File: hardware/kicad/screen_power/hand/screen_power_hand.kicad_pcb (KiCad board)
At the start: 2 copper layers, 68 x 76 mm, 48 parts, among them J1 AUX 5V INPUT, J101 PI USB / XH4, J102 TOUCH / XH4, J103 SCREEN 1 POWER, J2 GPIO17 / GND, J201 PI USB / XH4, J202 TOUCH / XH4, J203 SCREEN 2 POWER, K101 IM02TS, K201 IM02TS, Q1 2N3904, Q101 TN0702, Q2 2N3906, Q201 TN0702, Q3 SUP70101EL, Q4 SUP70101EL, U1 LMC7660IN, U2 TLP627M

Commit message: fix(hardware): finish revision M USB routing and manufacturing package
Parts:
- added Q102: TN0702, TO-92_Inline_Wide, F.Cu at (31.7, 45.7)
- added Q202: TN0702, TO-92_Inline_Wide, F.Cu at (31.7, 70.7)
- added R101: 10k 1%, R_Axial_DIN0207_L6.3mm_D2.5mm_P10.16mm_Horizontal, F.Cu at (22.1, 49.0)
- added R102: 100k 1%, R_Axial_DIN0207_L6.3mm_D2.5mm_P10.16mm_Horizontal, F.Cu at (32.8, 55.6)
- added R201: 10k 1%, R_Axial_DIN0207_L6.3mm_D2.5mm_P10.16mm_Horizontal, F.Cu at (9.42, 73.3)
- added R202: 100k 1%, R_Axial_DIN0207_L6.3mm_D2.5mm_P10.16mm_Horizontal, F.Cu at (22.1, 73.5)
- added TP101: SHIELD, TestPoint_THTPad_D2.0mm_Drill1.0mm, F.Cu at (13.5, 31.5)
- added TP102: SHIELD, TestPoint_THTPad_D2.0mm_Drill1.0mm, F.Cu at (51.5, 32.0)
- added TP201: SHIELD, TestPoint_THTPad_D2.0mm_Drill1.0mm, F.Cu at (13.5, 56.5)
- added TP202: SHIELD, TestPoint_THTPad_D2.0mm_Drill1.0mm, F.Cu at (51.5, 57.0)
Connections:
- C101 pad 1: HOST1_5V -> AUX_5V
- C201 pad 1: HOST2_5V -> AUX_5V
- D101 pad 1: HOST1_5V -> AUX_5V
- D201 pad 1: HOST2_5V -> AUX_5V
- K101 pad 1: HOST1_5V -> AUX_5V
- K201 pad 1: HOST2_5V -> AUX_5V
- Q101 pad 3: S1_DATA_COIL_LOW -> S1_RELAY_STACK
- Q201 pad 3: S2_DATA_COIL_LOW -> S2_RELAY_STACK
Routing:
- net AUX_5V: track 138.6 -> 200.5 mm, vias 0 -> 4
- net S2_HOST_PRESENT: track 0.00 -> 14.4 mm
- net S1_HOST_PRESENT: track 0.00 -> 13.7 mm
- net HOST2_5V: track 21.0 -> 9.45 mm
- net DATA_ENABLE: track 66.6 -> 76.8 mm
- net POWER_GATE: track 22.4 -> 28.1 mm
- net S2_RELAY_STACK: track 0.00 -> 4.69 mm
- net S1_RELAY_STACK: track 0.00 -> 4.69 mm
- net S1_DATA_COIL_LOW: track 29.4 -> 26.4 mm
- net S2_DATA_COIL_LOW: track 29.4 -> 26.4 mm
- net BUFFER_BASE: track 9.53 -> 11.4 mm
- net HOST1_5V: track 21.0 -> 19.2 mm
- net CONTROL_SINK: track 72.1 -> 71.3 mm
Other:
- board text added: "REV M"
- board text added: "SEGNO SCREEN POWER / REV M"
- board text removed: "REV L"
- board text removed: "SEGNO SCREEN POWER"
- board text removed: "SEGNO SCREEN POWER / REV L"

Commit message: fix(hardware): close Claude PCB review findings
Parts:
- R2: value 100k 1% -> 4.7k 1%
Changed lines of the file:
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@@
 			)
 		)
-		(property "Value" "100k 1%"
+		(property "Value" "4.7k 1%"
 			(at 5.08 2.37 0)
 			(layer "F.Fab")

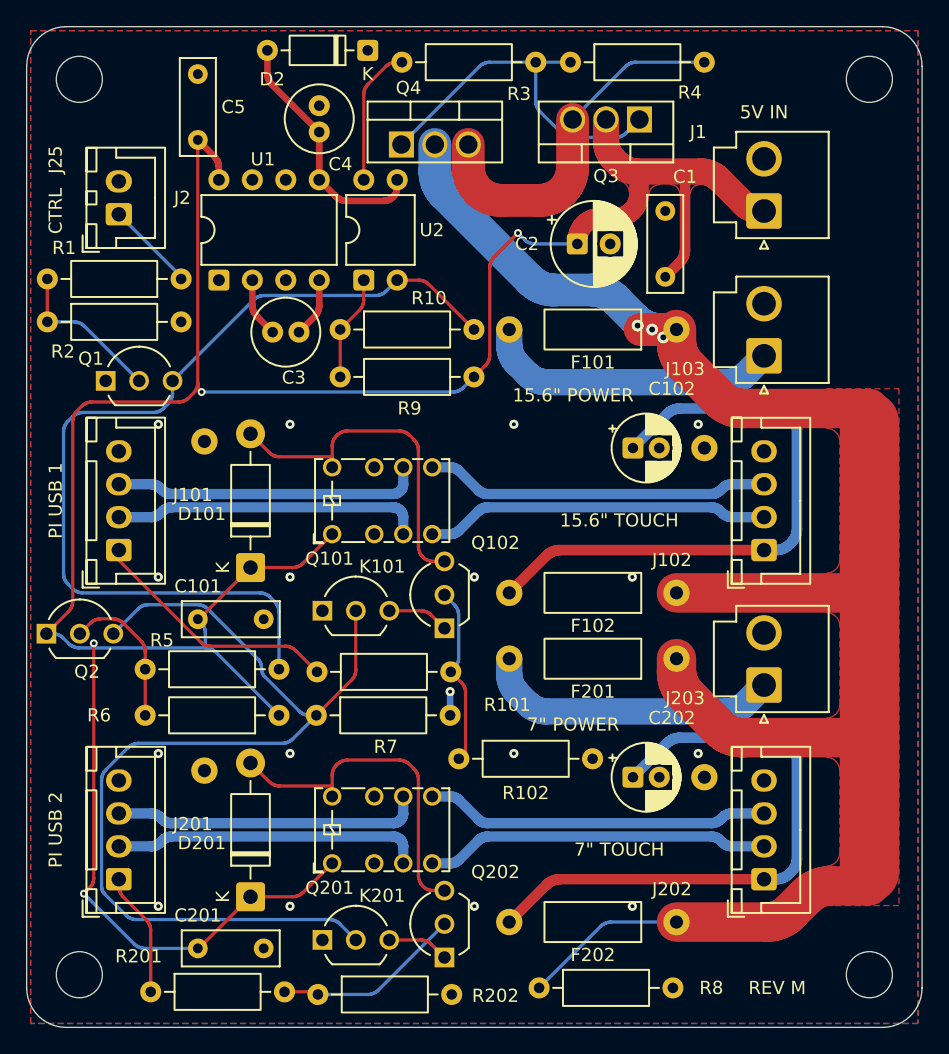
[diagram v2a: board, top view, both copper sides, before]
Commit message: feat(hardware): lower screen power cost and finish copper contours
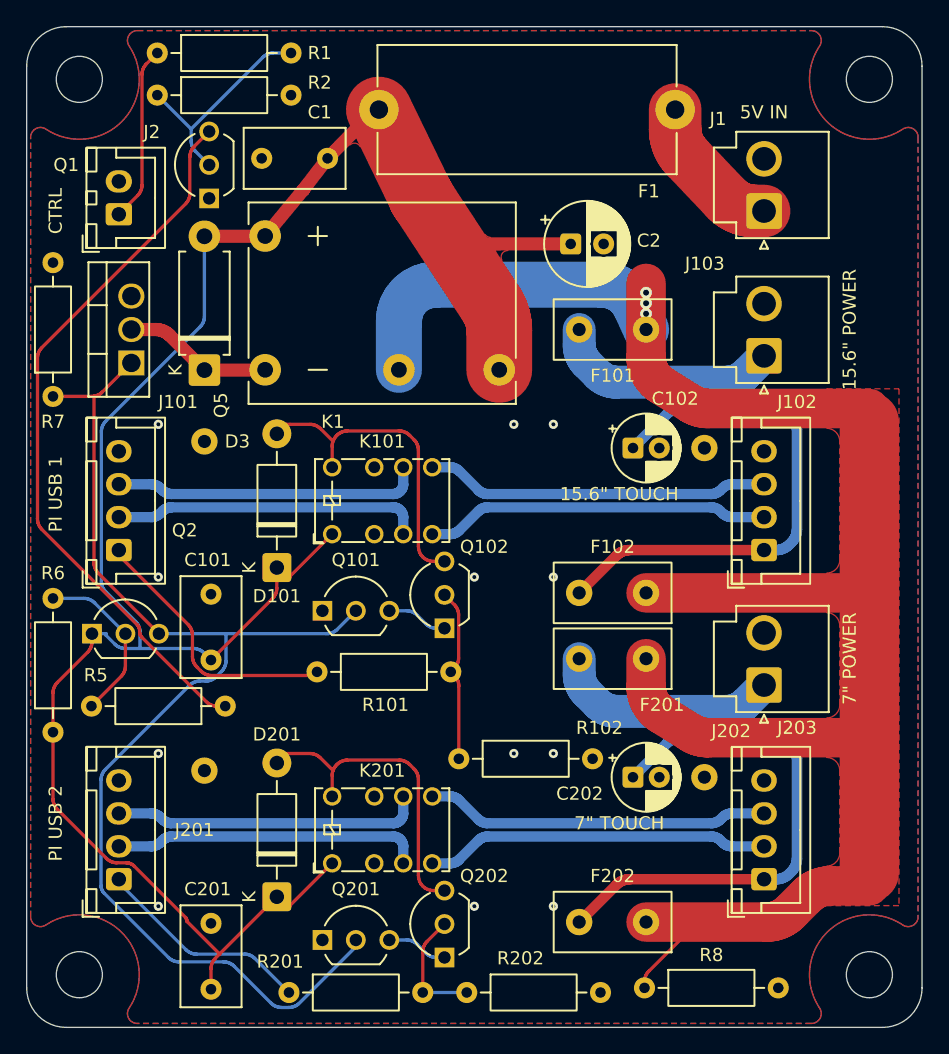
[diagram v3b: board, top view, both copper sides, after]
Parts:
- removed C3, C4: 10uF 25V bipolar, C_Radial_D5.0mm_H11.0mm_P2.00mm
- removed C5: 100nF 63V, C_Rect_L7.2mm_W2.5mm_P5.00mm
- removed D2: BAT85S, D_DO-35_SOD27_P7.62mm_Horizontal
- removed Q3, Q4: SUP70101EL, TO-220-3_SUP70101EL
- removed R10: 10k 1%, R_Axial_DIN0207_L6.3mm_D2.5mm_P10.16mm_Horizontal
- removed R3: 4.7k 1%, R_Axial_DIN0207_L6.3mm_D2.5mm_P10.16mm_Horizontal
- removed R4: 22k 1%, R_Axial_DIN0207_L6.3mm_D2.5mm_P10.16mm_Horizontal
- removed R9: 2.4k 1%, R_Axial_DIN0207_L6.3mm_D2.5mm_P10.16mm_Horizontal
- removed U1: LMC7660IN, DIP-8_W7.62mm
- removed U2: TLP627M, DIP-4_W7.62mm
- added D3: P6KE6.8CA, D_DO-15_P10.16mm_Horizontal, F.Cu at (13.5, 26.1)
- added F1: 8A time-lag, Fuseholder_Schurter_OGN_0031.8201, F.Cu at (49.2, 6.30)
- added K1: G6C-1117P-US, Relay_Omron_G6C-1117P-US, F.Cu at (18.1, 26.1)
- added Q5: IRLZ44N, TO-220-3_IRLZ44N, F.Cu at (7.95, 25.5)
- C1, C101, C201: value 100nF 63V -> 100nF 50V X7R; footprint C_Rect_L7.2mm_W2.5mm_P5.00mm -> C_Disc_D7.5mm_W4.4mm_P5.00mm
- F101, F201: value 4A fast -> 4A time-lag; footprint Fuse_Littelfuse_251_P12.70mm -> Fuse_Bel_0697H_P5.08mm
- F102, F202: value 750mA fast -> 800mA time-lag; footprint Fuse_Littelfuse_251_P12.70mm -> Fuse_Bel_0697H_P5.08mm
- R7: value 100k 1% -> 10k 1%
- moved R7 31.4 mm to (2.00, 28.1), turned to 90 degrees
- moved C1 27.2 mm to (22.9, 10.0), turned to 180 degrees
- moved R2 19.1 mm to (9.92, 5.20)
- moved R1 17.3 mm to (9.92, 2.00), turned to 0 degrees
- moved R6 17.2 mm to (2.00, 53.6), turned to 90 degrees
- moved Q1 15.9 mm to (13.9, 13.0), turned to 90 degrees
- moved R202 11.3 mm to (33.4, 73.3)
- moved R201 10.5 mm to (19.9, 73.3)
- moved R8 8.00 mm to (46.9, 73.0)
- moved R5 4.95 mm to (15.1, 51.6)
- moved Q2 3.46 mm to (4.96, 46.1)
- moved C101 3.26 mm to (14.0, 48.1), turned to 90 degrees
- moved C201 3.26 mm to (14.0, 73.1), turned to 90 degrees
- moved F101 2.31 mm to (47.0, 23.0)
- moved F102 2.31 mm to (47.0, 43.0)
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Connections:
- J1 pad 1: AUX_5V -> AUX_5V_IN
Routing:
- net AUX_5V: track 200.5 -> 154.9 mm, vias 4 -> 0
- net POWER_GATE: track 28.1 -> 0.00 mm
- net COMMON_SOURCE: track 27.9 -> 0.00 mm
- net NEG_5V: track 19.1 -> 0.00 mm
- net CONTROL_SINK: track 71.3 -> 55.3 mm
- net DATA_ENABLE: track 76.8 -> 91.9 mm
- net POWER_COIL_LOW: track 0.00 -> 11.4 mm
- net AUX_5V_IN: track 0.00 -> 11.3 mm
- net GATE_SINK: track 10.6 -> 0.00 mm
- net GATE_LED: track 8.04 -> 0.00 mm
- net HOST2_5V: track 9.45 -> 16.5 mm
- net PI_GPIO17: track 6.87 -> 13.4 mm
- net S2_TOUCH_5V: track 46.1 -> 40.8 mm
- net S2_MAIN_5V: track 22.7 -> 17.4 mm
- net S1_TOUCH_5V: track 46.1 -> 40.8 mm
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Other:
- board text added: "SEGNO SCREEN POWER / REV N"
- board text removed: "J25"
- board text removed: "REV M"
- board text removed: "SEGNO SCREEN POWER / REV M"

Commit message: feat(hardware): carry USB shields through removable XH5 plugs
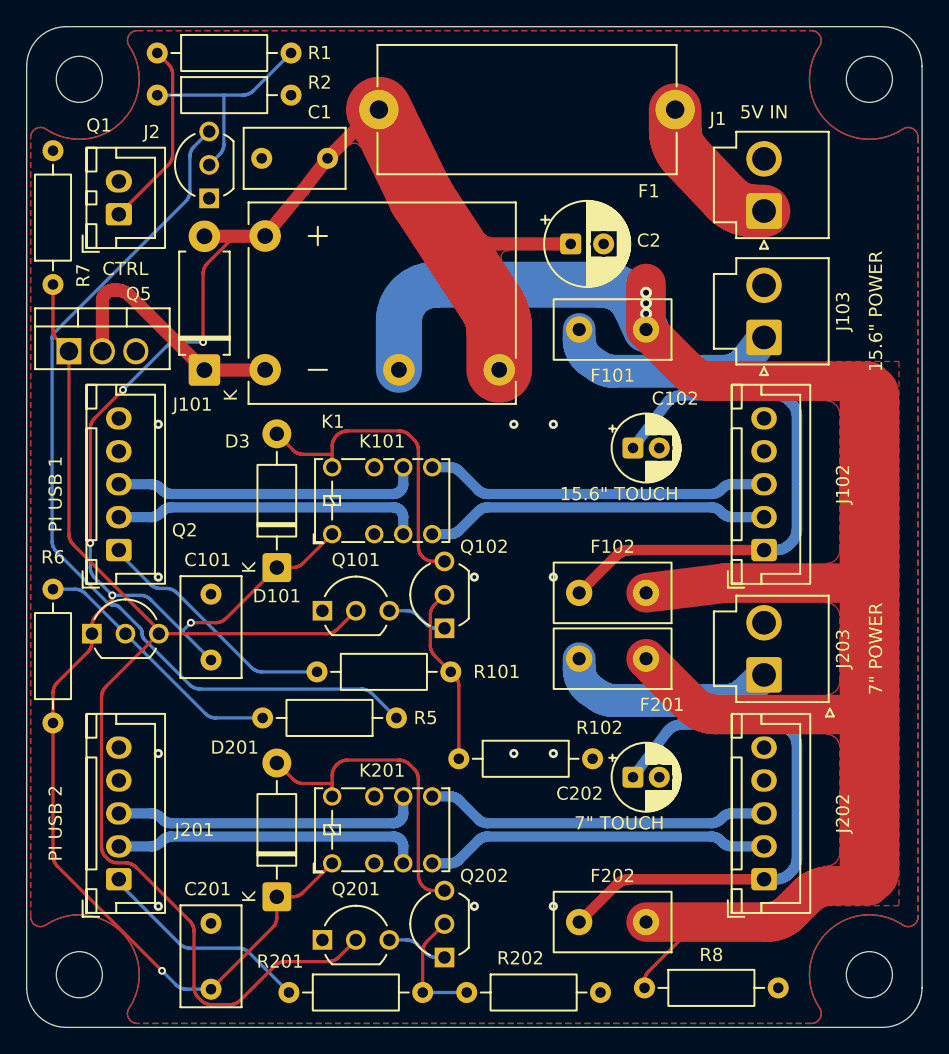
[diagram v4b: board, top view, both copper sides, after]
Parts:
- removed TP101, TP102, TP201, TP202: SHIELD, TestPoint_THTPad_D2.0mm_Drill1.0mm
- J101, J201: value PI USB / XH4 -> PI USB / XH5; footprint JST_XH_B4B-XH-A_1x04_P2.50mm_Vertical -> JST_XH_B5B-XH-A_1x05_P2.50mm_Vertical
- J102, J202: value TOUCH / XH4 -> TOUCH / XH5; footprint JST_XH_B4B-XH-A_1x04_P2.50mm_Vertical -> JST_XH_B5B-XH-A_1x05_P2.50mm_Vertical
- moved R5 13.0 mm to (28.1, 52.5)
- moved R7 8.50 mm to (2.00, 19.6)
- moved Q5 4.82 mm to (3.21, 24.6), turned to 0 degrees
- moved J103 1.40 mm to (56.0, 23.6)
- moved J203 0.77 mm to (56.0, 49.2)
- moved R6 0.70 mm to (2.00, 52.9)
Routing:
- net CONTROL_SINK: track 55.3 -> 68.0 mm
- net POWER_COIL_LOW: track 11.4 -> 19.1 mm
- net BUFFER_BASE: track 13.1 -> 19.9 mm
- net AUX_5V: track 154.9 -> 159.6 mm, vias 0 -> 6
- net SWITCHED_5V: track 146.9 -> 144.3 mm
- net HOST1_5V: track 20.7 -> 18.9 mm
- net S1_TOUCH_5V: track 40.8 -> 42.5 mm
- net S2_TOUCH_5V: track 40.8 -> 42.5 mm
- net PI_GPIO17: track 13.4 -> 14.3 mm
- net S2_MAIN_5V: track 17.4 -> 16.8 mm
- net DATA_ENABLE: track 91.9 -> 92.5 mm
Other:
- board text added: "5 SHLD"
- board text added: "SEGNO SCREEN POWER / REV O"
- board text removed: "SEGNO SCREEN POWER / REV N"

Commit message: fix(hardware): smooth screen power ground at H1
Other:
- board text added: "SEGNO SCREEN POWER / REV P"
- board text removed: "SEGNO SCREEN POWER / REV O"
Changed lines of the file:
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@@
 	(title_block
 		(title "Segno screen power")
-		(rev "O")
+		(rev "P")
 	)
 	(layers
@@
 		)
 	)
-	(gr_text "SEGNO SCREEN POWER / REV O"
+	(gr_text "SEGNO SCREEN POWER / REV P"
 		(at 47 75 0)
 		(layer "B.SilkS")
@@
 	(zone
 		(layer "F.Cu")
-		(name "GROUND_TIP_CLEARANCE")
-		(hatch edge 0.5)
-		(connect_pads
-			(clearance 0)
-		)
-		(min_thickness 0.25)
-		(keepout
-			(tracks allowed)
-			(vias allowed)
-			(pads allowed)
-			(copperpour not_allowed)
-			(footprints allowed)
-		)
-		(placement
-			(enabled no)
-			(sheetname "")
-		)
-		(fill
-			(thermal_gap 0.5)
-			(thermal_bridge_width 0.5)
-			(island_removal_mode 0)
-		)
-		(polygon
-			(pts
-				(xy 8.9195 1.980935) (xy 8.918574 2.008129) (xy 8.915802 2.035197) (xy 8.911196 2.062013) (xy 8.904778 2.088455)
-				(xy 8.896577 2.114399) (xy 8.886631 2.139725) (xy 8.874987 2.164317) (xy 8.861698 2.18806) (xy 8.846825 2.210844)
-				(xy 8.830437 2.232565) (xy 8.812611 2.253122) (xy 8.793429 2.272419) (xy 8.772979 2.290367) (xy 8.751356 2.306884)
-				(xy 8.728661 2.321892) (xy 8.704997 2.335323) (xy 8.680475 2.347114) (xy 8.655209 2.357211) (xy 8.629314 2.365566)
-				(xy 8.602912 2.372142) (xy 8.576123 2.376907) (xy 8.549072 2.379841) (xy 8.521885 2.380928) (xy 8.494686 2.380165)
-				(xy 8.467603 2.377555) (xy 8.440759 2.373109) (xy 8.41428 2.366848) (xy 8.388287 2.358802) (xy 8.362902 2.349008)
-				(xy 8.338241 2.33751) (xy 8.31442 2.324363) (xy 8.291547 2.309626) (xy 8.269728 2.293368) (xy 8.249066 2.275665)
-				(xy 8.229655 2.256598) (xy 8.211585 2.236256) (xy 8.194939 2.214732) (xy 8.179796 2.192126) (xy 8.166224 2.168543)
-				(xy 8.154287 2.144092) (xy 7.8 3.5) (xy 9.02 3.5) (xy 9.02 1.980935)
-			)
-		)
-	)
-	(zone
-		(layer "F.Cu")
 		(hatch edge 0.5)
 		(connect_pads
@@
 			)
 		)
-	)
-	(zone
-		(layer "F.Cu")
-		(name "GROUND_TIP_CLEARANCE")
-		(hatch edge 0.5)
-		(connect_pads
-			(clearance 0)
-		)
-		(min_thickness 0.25)
-		(keepout
-			(tracks allowed)
-			(vias allowed)
-			(pads allowed)
-			(copperpour not_allowed)
-			(footprints allowed)
-		)
-		(placement
-			(enabled no)
-			(sheetname "")
-		)
-		(fill
-			(thermal_gap 0.5)
-			(thermal_bridge_width 0.5)
-			(island_removal_mode 0)
-		)
-		(polygon
-			(pts
-				(xy 8.4347 6.867698) (xy 8.433904 6.842478) (xy 8.431519 6.817358) (xy 8.427556 6.792439) (xy 8.422029 6.767819)
-				(xy 8.414961 6.743597) (xy 8.40638 6.719868) (xy 8.39632 6.696728) (xy 8.38482 6.674267) (xy 8.371928 6.652577)
-				(xy 8.357693 6.631743) (xy 8.342174 6.611847) (xy 8.325431 6.59297) (xy 8.30753 6.575186) (xy 8.288545 6.558566)
-				(xy 8.268549 6.543176) (xy 8.247622 6.529078) (xy 8.225849 6.516327) (xy 8.203314 6.504974) (xy 8.180109 6.495064)
-				(xy 8.156325 6.486637) (xy 8.132057 6.479727) (xy 8.107402 6.474361) (xy 8.082457 6.470559) (xy 8.057322 6.468338)
-				(xy 8.032097 6.467707) (xy 8.006883 6.468667) (xy 7.981779 6.471214) (xy 7.956886 6.47534) (xy 7.932303 6.481027)
-				(xy 7.908127 6.488252) (xy 7.884455 6.496987) (xy 7.86138 6.507198) (xy 7.838995 6.518843) (xy 7.817389 6.531876)
-				(xy 7.796648 6.546246) (xy 7.776854 6.561895) (xy 7.758086 6.57876) (xy 7.740419 6.596776) (xy 7.723923 6.615869)
-				(xy 7.708663 6.635965) (xy 7.8 4.3) (xy 8.7 4.3) (xy 8.7 6.867698)
-			)
-		)
